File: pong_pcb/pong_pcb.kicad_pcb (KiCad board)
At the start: 4 copper layers, 100 x 100 mm, 87 parts, among them J1 Screw_Terminal_01x02, J2 685119134923, J3 Screw_Terminal_01x03, J4 Screw_Terminal_01x03, J5 Screw_Terminal_01x02, J6 Screw_Terminal_01x05, J7 Screw_Terminal_01x05, J8 Screw_Terminal_01x02, U1 LMR23630APQDRRTQ1, U3 TPD12S016RKTR, U4 MAX17626ATA+T, U5 SN74LVC2G34DBV, U6 SN74LVC2G34DBV, U7 SN74LVC2G34DBV, U8 SN74LVC2G34DBV, U9 SN74LVC2G34DBV

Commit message: PCB indeling maken
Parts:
- added H1: MountingHole_Pad, MountingHole:MountingHole_3.2mm_M3_Pad_Via, F.Cu at (65.0, 49.0)
- added H2: MountingHole_Pad, MountingHole:MountingHole_3.2mm_M3_Pad_Via, F.Cu at (155.0, 49.0)
- added H3: MountingHole_Pad, MountingHole:MountingHole_3.2mm_M3_Pad_Via, F.Cu at (65.0, 139.0)
- added H4: MountingHole_Pad, MountingHole:MountingHole_3.2mm_M3_Pad_Via, F.Cu at (155.0, 139.0)
- moved C25 284.7 mm to (137.8, 68.5), turned to 180 degrees
- moved RV10 283.5 mm to (147.5, 60.3), turned to 90 degrees
- moved R18 281.8 mm to (146.0, 63.3), turned to -90 degrees
- moved R23 280.4 mm to (147.5, 63.3), turned to 90 degrees
- moved U9 280.4 mm to (142.2, 68.5), turned to 180 degrees
- moved J8 278.8 mm to (154.0, 59.0), turned to -90 degrees
- moved RV5 269.3 mm to (147.5, 74.2), turned to 90 degrees
- moved R10 267.9 mm to (146.0, 77.2), turned to 90 degrees
- moved R15 266.4 mm to (147.5, 77.2), turned to 90 degrees
- moved J5 264.1 mm to (154.0, 73.0), turned to -90 degrees
- moved C22 257.9 mm to (133.6, 116.0), turned to 180 degrees
- moved U6 252.8 mm to (138.0, 116.0), turned to 180 degrees
- moved R8 250.5 mm to (143.0, 111.7), turned to -90 degrees
- moved D3 248.9 mm to (95.0, 125.1)
- moved D4 248.9 mm to (100.0, 125.1)
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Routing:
- net +5V: track 42.3 -> 65.8 mm, vias 3 -> 4
- net /5v-PSU/v-in: track 6.65 -> 23.9 mm
- net GND: track 187.1 -> 196.0 mm, vias 84 -> 90
- net VU: track 0.00 -> 6.64 mm
- net +3.3V: track 132.8 -> 128.2 mm
- added copper zone on F.Cu, net +5V
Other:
- outline, holes or cut-outs redrawn

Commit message: Update schema and route PCB
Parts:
- added C13: 47u 10v, Capacitor_SMD:C_1206_3216Metric_Pad1.33x1.80mm_HandSolder, F.Cu at (139.4, 109.0)
- added C22: 100n 10v, Capacitor_SMD:C_0603_1608Metric, F.Cu at (92.0, 127.0)
- added C23: 100n 10v, Capacitor_SMD:C_0603_1608Metric, F.Cu at (103.0, 127.0)
- added C24: 100n 10v, Capacitor_SMD:C_0603_1608Metric, F.Cu at (132.0, 127.0)
- added C25: 100n 10v, Capacitor_SMD:C_0603_1608Metric, F.Cu at (143.0, 127.0)
- added C26: 47u 10v, Capacitor_SMD:C_1206_3216Metric_Pad1.33x1.80mm_HandSolder, F.Cu at (110.0, 137.1)
- moved C31 1.49 mm to (138.8, 69.6), turned to -90 degrees
- renumbered C13 to C14, C14 to C15, C15 to C16, C16 to C17, C17 to C18, C18 to C19, C19 to C20, C20 to C21, C21 to C27, C22 to C28, C23 to C29, C24 to C30, C25 to C31
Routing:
- net +3.3V: track 128.2 -> 454.7 mm, vias 3 -> 8
- net +5V: track 65.8 -> 321.1 mm, vias 4 -> 8
- net /FPGA_HDMI/GameReset: track 0.00 -> 82.5 mm
- net /FPGA_HDMI/Controller_switch: track 0.00 -> 78.1 mm
- net /FPGA_HDMI/BTN_up_l: track 0.00 -> 55.4 mm, vias 0 -> 1
- net /FPGA_HDMI/BTN_down_l: track 0.00 -> 52.0 mm, vias 0 -> 1
- net /FPGA_HDMI/Sensor_l: track 0.00 -> 34.6 mm, vias 0 -> 2
- net /FPGA_HDMI/Trigger_r: track 0.00 -> 34.0 mm, vias 0 -> 2
- net /FPGA_HDMI/Trigger_l: track 0.00 -> 29.0 mm, vias 0 -> 2
- net GND: track 196.0 -> 224.5 mm, vias 90 -> 103
- net /FPGA_HDMI/Sensor_r: track 0.00 -> 26.3 mm
- net /FPGA_HDMI/BTN_down_r: track 0.00 -> 25.0 mm, vias 0 -> 2
- net /FPGA_HDMI/BTN_up_r: track 0.00 -> 20.5 mm
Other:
- board text added: "TODO: HDMI vias om de max 2 cm"

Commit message: Other connectors
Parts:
- J1: footprint TerminalBlock_Phoenix:TerminalBlock_Phoenix_MKDS-3-2-5.08_1x02_P5.08mm_Horizontal -> Connector_Phoenix_MSTB:PhoenixContact_MSTBA_2,5_2-G-5,08_1x02_P5.08mm_Horizontal
- J3, J4: footprint TerminalBlock_Phoenix:TerminalBlock_Phoenix_MKDS-1,5-3-5.08_1x03_P5.08mm_Horizontal -> Connector_Phoenix_MSTB:PhoenixContact_MSTBA_2,5_3-G-5,08_1x03_P5.08mm_Horizontal
- J5, J8: footprint TerminalBlock_Phoenix:TerminalBlock_Phoenix_MKDS-1,5-2-5.08_1x02_P5.08mm_Horizontal -> Connector_Phoenix_MSTB:PhoenixContact_MSTBA_2,5_2-G-5,08_1x02_P5.08mm_Horizontal
- J6, J7: footprint TerminalBlock_Phoenix:TerminalBlock_Phoenix_MKDS-1,5-5-5.08_1x05_P5.08mm_Horizontal -> Connector_Phoenix_MSTB:PhoenixContact_MSTBA_2,5_5-G-5,08_1x05_P5.08mm_Horizontal
- moved J7 20.4 mm to (119.6, 133.8), turned to 0 degrees
- moved J6 20.3 mm to (79.7, 133.8), turned to 0 degrees
- moved J4 10.1 mm to (149.8, 121.1), turned to 90 degrees
- moved J3 10.1 mm to (70.2, 111.0), turned to -90 degrees
- moved J8 6.85 mm to (150.0, 64.5), turned to 90 degrees
- moved J5 6.42 mm to (150.0, 78.0), turned to 90 degrees
- moved J1 6.15 mm to (97.0, 54.0), turned to 180 degrees
- moved R10 1.50 mm to (144.5, 77.2)
- moved R15 1.50 mm to (146.0, 77.2)
- moved R18 1.50 mm to (144.5, 63.3)
- moved R23 1.50 mm to (146.0, 63.3)
- moved RV10 1.50 mm to (146.0, 60.3)
- moved RV5 1.50 mm to (146.0, 74.2)
- moved D1 0.50 mm to (94.3, 70.0)
- moved D2 0.50 mm to (92.0, 62.6)
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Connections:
- net Net-(D1-A) renamed /power_fused
- F1 pad 1: Net-(J1-Pin_2) -> /power_in
- J1 pad 1: GND -> /power_in
- J1 pad 2: Net-(J1-Pin_2) -> GND
- J3 pad 1: /SignalBuffer/ButtonDown1 -> /SignalBuffer/ButtonUp1
- J3 pad 3: /SignalBuffer/ButtonUp1 -> /SignalBuffer/ButtonDown1
- J4 pad 1: /SignalBuffer/ButtonDown2 -> /SignalBuffer/ButtonUp2
- J4 pad 3: /SignalBuffer/ButtonUp2 -> /SignalBuffer/ButtonDown2
- J5 pad 1: GND -> /SignalBuffer/ControllerSelect
- J5 pad 2: /SignalBuffer/ControllerSelect -> GND
- J6 pad 1: +5V -> /SignalBuffer/Echo1
- J6 pad 2: +3.3V -> GND
- J6 pad 4: GND -> +3.3V
- J6 pad 5: /SignalBuffer/Echo1 -> +5V
- J7 pad 1: +5V -> /SignalBuffer/Echo2
- J7 pad 2: +3.3V -> GND
- J7 pad 4: GND -> +3.3V
- J7 pad 5: /SignalBuffer/Echo2 -> +5V
- J8 pad 1: GND -> /SignalBuffer/GameReset
- J8 pad 2: /SignalBuffer/GameReset -> GND
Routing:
- net GND: track 224.5 -> 228.5 mm
- net /SignalBuffer/GameReset: track 12.8 -> 9.74 mm
- net /SignalBuffer/ControllerSelect: track 16.7 -> 14.0 mm
- net +3.3V: track 454.7 -> 453.2 mm
- net Hdmi_out_clk+: track 48.4 -> 49.2 mm
- net Hdmi_out_clk-: track 48.3 -> 49.0 mm
- net Hdmi_out_data_0-: track 48.4 -> 48.9 mm
- net Hdmi_out_data_0+: track 47.0 -> 47.5 mm
- added copper zone on F.Cu, net /power_in
- removed copper zone on F.Cu, net Net-(J1-Pin_2)
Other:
- board text added: "Echo | GND | Trig | 3.3v | 5v"
- board text added: "Up | GND | Down"

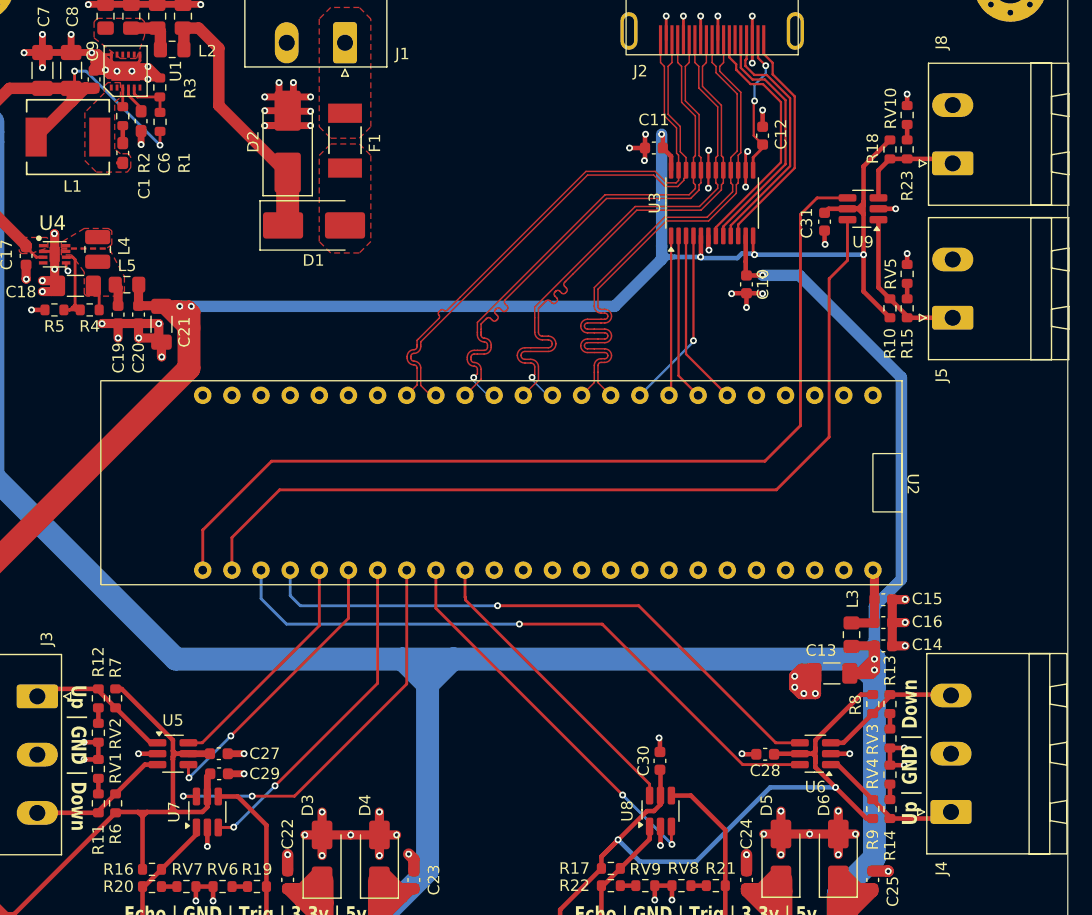
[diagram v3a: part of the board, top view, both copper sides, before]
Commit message: Add header pins
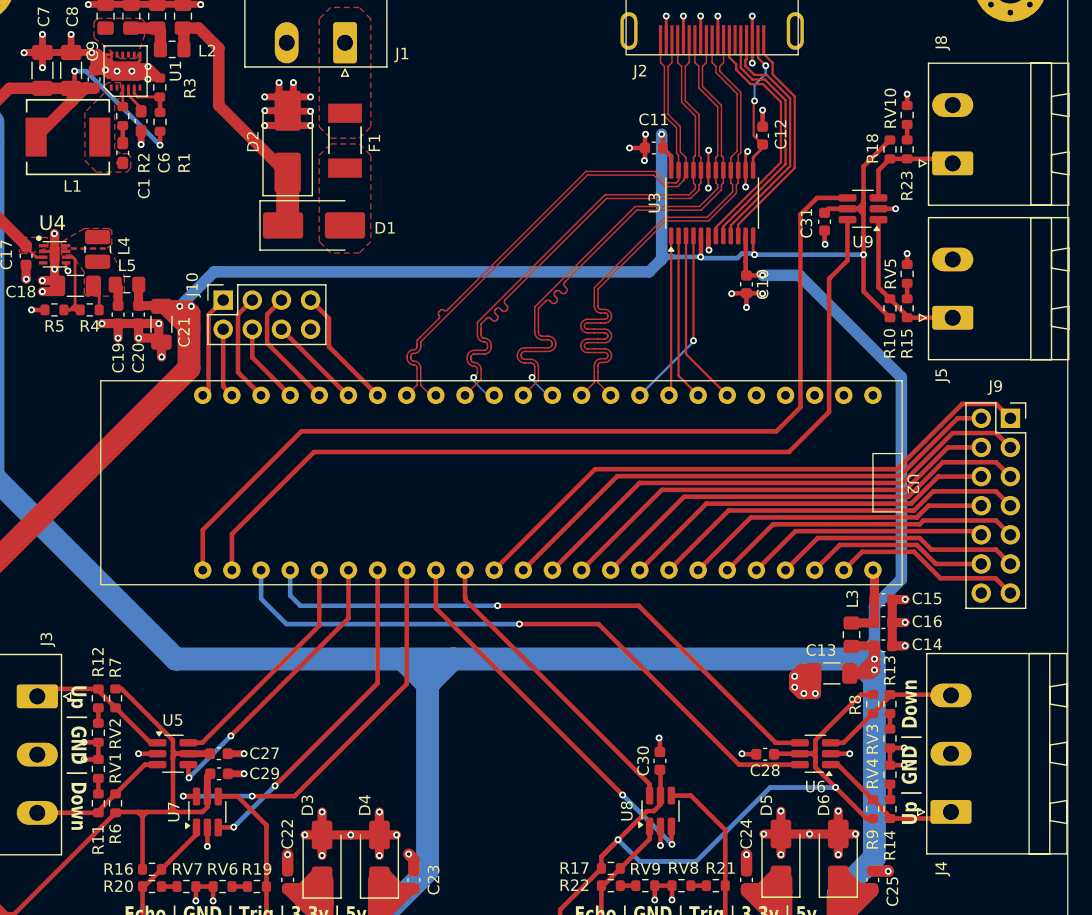
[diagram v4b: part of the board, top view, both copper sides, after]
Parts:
- added J10: Conn_01x07_Socket, Connector_PinSocket_2.54mm:PinSocket_2x04_P2.54mm_Vertical, F.Cu at (86.4, 76.5)
- added J9: Conn_01x13_Socket, Connector_PinSocket_2.54mm:PinSocket_2x07_P2.54mm_Vertical, F.Cu at (155.0, 86.8)
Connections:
- U2 pad 11: unconnected-(U2-pio11-Pad11) -> Net-(J9-Pin_1)
- U2 pad 12: unconnected-(U2-pio12-Pad12) -> Net-(J9-Pin_2)
- U2 pad 13: unconnected-(U2-pio13-Pad13) -> Net-(J9-Pin_3)
- U2 pad 14: unconnected-(U2-pio14-Pad14) -> Net-(J9-Pin_4)
- U2 pad 15: unconnected-(U2-pio15-Pad15) -> Net-(J9-Pin_5)
- U2 pad 16: unconnected-(U2-pio16-Pad16) -> Net-(J9-Pin_6)
- U2 pad 17: unconnected-(U2-pio17-Pad17) -> Net-(J9-Pin_7)
- U2 pad 18: unconnected-(U2-pio18-Pad18) -> Net-(J9-Pin_8)
- U2 pad 19: unconnected-(U2-pio19-Pad19) -> Net-(J9-Pin_9)
- U2 pad 20: unconnected-(U2-pio20-Pad20) -> Net-(J9-Pin_10)
- U2 pad 21: unconnected-(U2-pio21-Pad21) -> Net-(J9-Pin_11)
- U2 pad 22: unconnected-(U2-pio22-Pad22) -> Net-(J9-Pin_12)
- U2 pad 23: unconnected-(U2-pio23-Pad23) -> Net-(J9-Pin_13)
- U2 pad 42: unconnected-(U2-pio42-Pad42) -> Net-(J10-Pin_7)
- U2 pad 43: unconnected-(U2-pio43-Pad43) -> Net-(J10-Pin_6)
- U2 pad 44: unconnected-(U2-pio44-Pad44) -> Net-(J10-Pin_5)
- U2 pad 45: unconnected-(U2-pio45-Pad45) -> Net-(J10-Pin_4)
- U2 pad 46: unconnected-(U2-pio46-Pad46) -> Net-(J10-Pin_3)
- U2 pad 47: unconnected-(U2-pio47-Pad47) -> Net-(J10-Pin_2)
- U2 pad 48: unconnected-(U2-pio48-Pad48) -> Net-(J10-Pin_1)
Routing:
- net Net-(J9-Pin_1): track 0.00 -> 51.5 mm
- net Net-(J9-Pin_2): track 0.00 -> 45.4 mm
- net Net-(J9-Pin_3): track 0.00 -> 45.4 mm
- net Net-(J9-Pin_4): track 0.00 -> 39.3 mm
- net Net-(J9-Pin_5): track 0.00 -> 39.3 mm
- net Net-(J9-Pin_6): track 0.00 -> 33.1 mm
- net Net-(J9-Pin_7): track 0.00 -> 33.1 mm
- net Net-(J9-Pin_8): track 0.00 -> 27.0 mm
- net Net-(J9-Pin_9): track 0.00 -> 27.0 mm
- net Net-(J9-Pin_11): track 0.00 -> 21.7 mm
- net Net-(J9-Pin_10): track 0.00 -> 21.1 mm
- net Net-(J9-Pin_13): track 0.00 -> 16.7 mm
- net Net-(J9-Pin_12): track 0.00 -> 16.1 mm
- net Net-(J10-Pin_7): track 0.00 -> 10.7 mm
- net Net-(J10-Pin_5): track 0.00 -> 10.7 mm
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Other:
- board text added: "TODO: HDMI vias om de max 2 cm NAME"
- board text removed: "TODO: HDMI vias om de max 2 cm"

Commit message: Update TODOs
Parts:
- removed J10: Conn_01x07_Socket, Connector_PinSocket_2.54mm:PinSocket_2x04_P2.54mm_Vertical
- added J11: Conn_01x08_Socket, Connector_PinSocket_2.54mm:PinSocket_2x04_P2.54mm_Vertical, F.Cu at (86.4, 76.5)
- J9: value Conn_01x13_Socket -> Conn_01x14_Socket
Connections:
- J9 pad 14: (no net) -> GND
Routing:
- net Net-(J11-Pin_6): track 10.7 -> 7.09 mm
- net Net-(J11-Pin_4): track 9.65 -> 6.05 mm
- net Net-(J11-Pin_3): track 6.07 -> 9.00 mm
- net Net-(J11-Pin_2): track 9.04 -> 6.46 mm
- net Net-(J11-Pin_8): track 10.7 -> 8.21 mm
- net Net-(J11-Pin_5): track 7.13 -> 9.61 mm
- net Net-(J11-Pin_7): track 8.23 -> 10.7 mm
- net GND: vias 103 -> 254
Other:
- board text added: "+"
- board text added: "6V-36V"
- board text added: "FPGA Pong game"
- board text added: "Jochem Bosman Tommy de Wever"
- board text added: "Reset game"
- board text added: "Select controller"
- board text added: "TODO:"
- board text added: "V1.0 19-6-2024"
- board text added: "_"
- board text removed: "TODO: HDMI vias om de max 2 cm NAME"

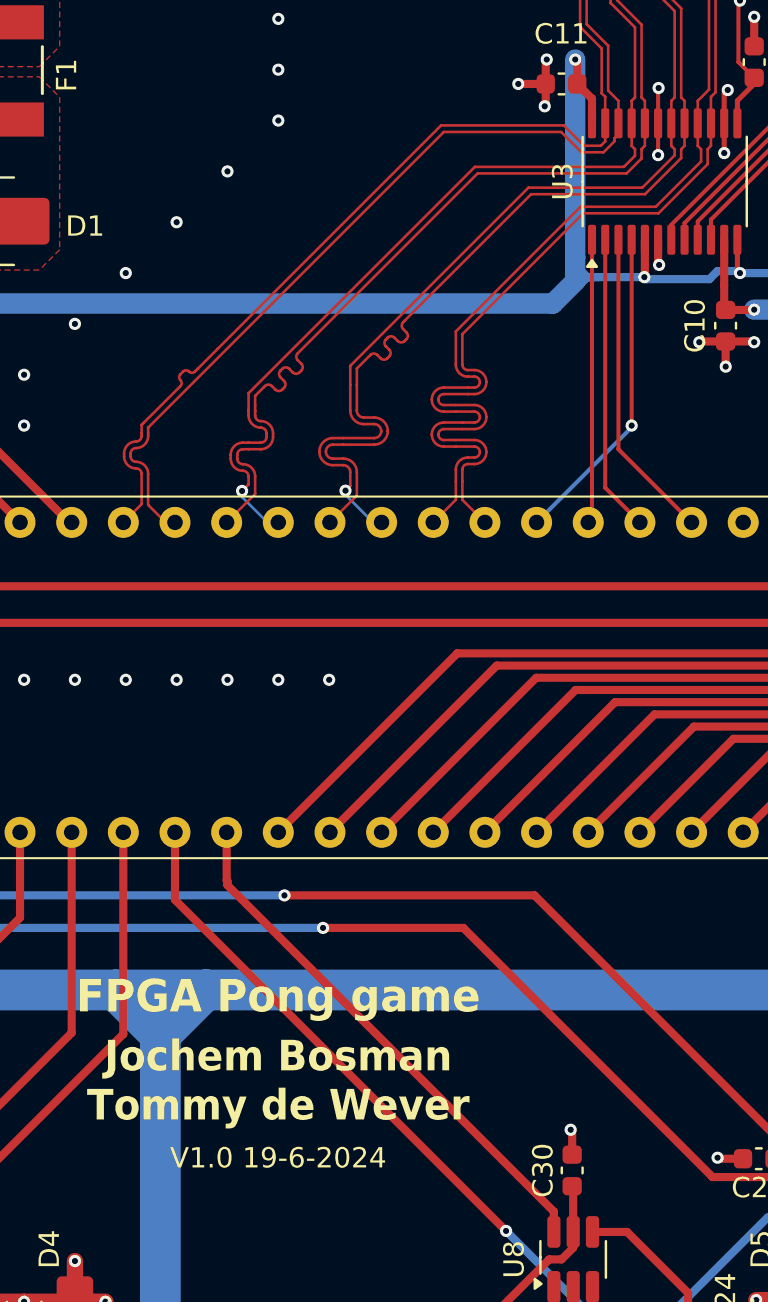
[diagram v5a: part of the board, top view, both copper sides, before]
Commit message: Fix HDMI pinout
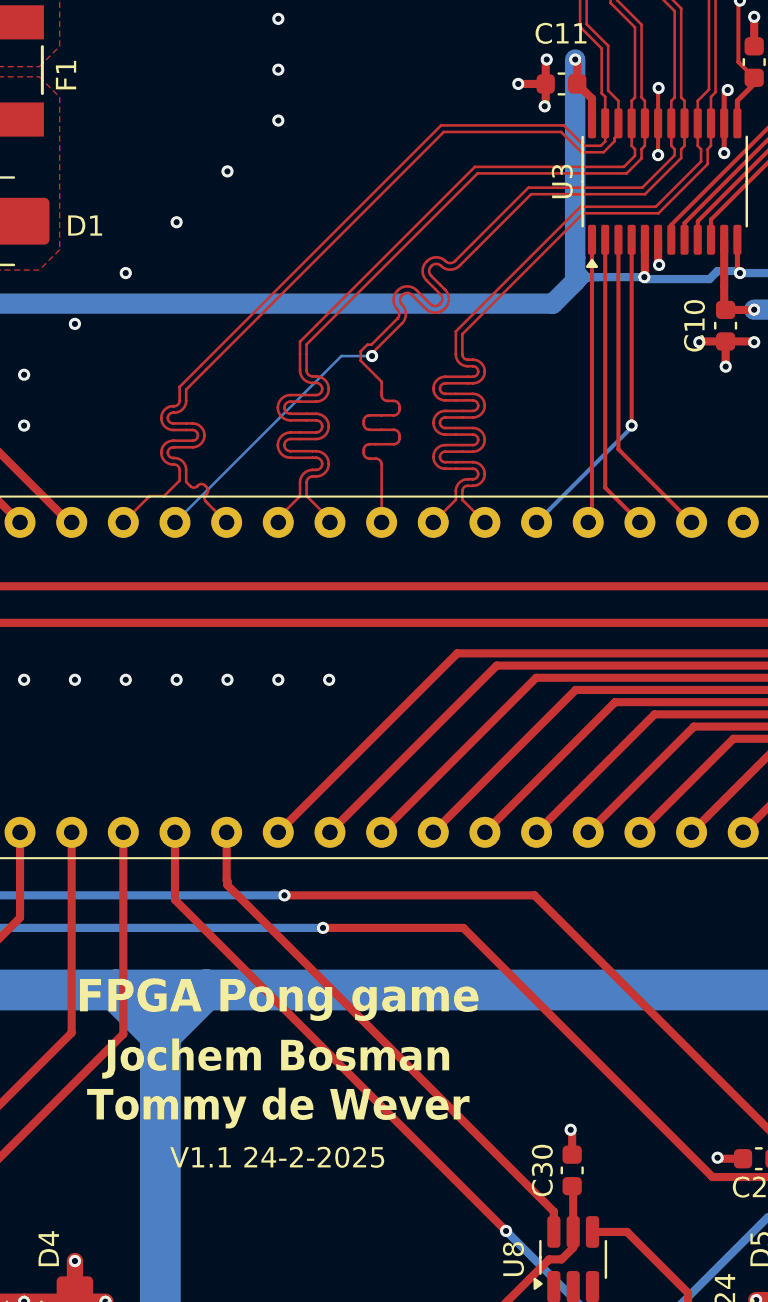
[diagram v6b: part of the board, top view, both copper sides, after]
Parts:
- C17: value 2.2uF -> 2.2u
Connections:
- U2 pad 37: Hdmi_out_data_0- -> Hdmi_out_data_1-
- U2 pad 39: Hdmi_out_data_1- -> Hdmi_out_data_2-
- U2 pad 40: Hdmi_out_data_2- -> Hdmi_out_data_0-
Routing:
- net Hdmi_out_data_0+: track 47.5 -> 51.8 mm, vias 1 -> 0
- net Hdmi_out_data_1+: track 47.4 -> 51.6 mm, vias 1 -> 0
- net Hdmi_out_data_1-: track 48.8 -> 51.6 mm
- net Hdmi_out_data_2+: track 48.8 -> 51.7 mm
- net Hdmi_out_clk+: track 49.2 -> 52.0 mm
- net Hdmi_out_clk-: track 49.0 -> 51.9 mm
- net Hdmi_out_data_2-: track 49.1 -> 51.8 mm
- net Hdmi_out_data_0-: track 48.9 -> 50.4 mm, vias 0 -> 1
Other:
- board text added: "V1.1 24-2-2025"
- board text removed: "V1.0 19-6-2024"
